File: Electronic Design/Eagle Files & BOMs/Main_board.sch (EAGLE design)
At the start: 42 parts, among them IC2 ATMEGA328-PU, IC3 LM2576S, Q1 IRF9540, Q2 IRF9540, X1 16MHz

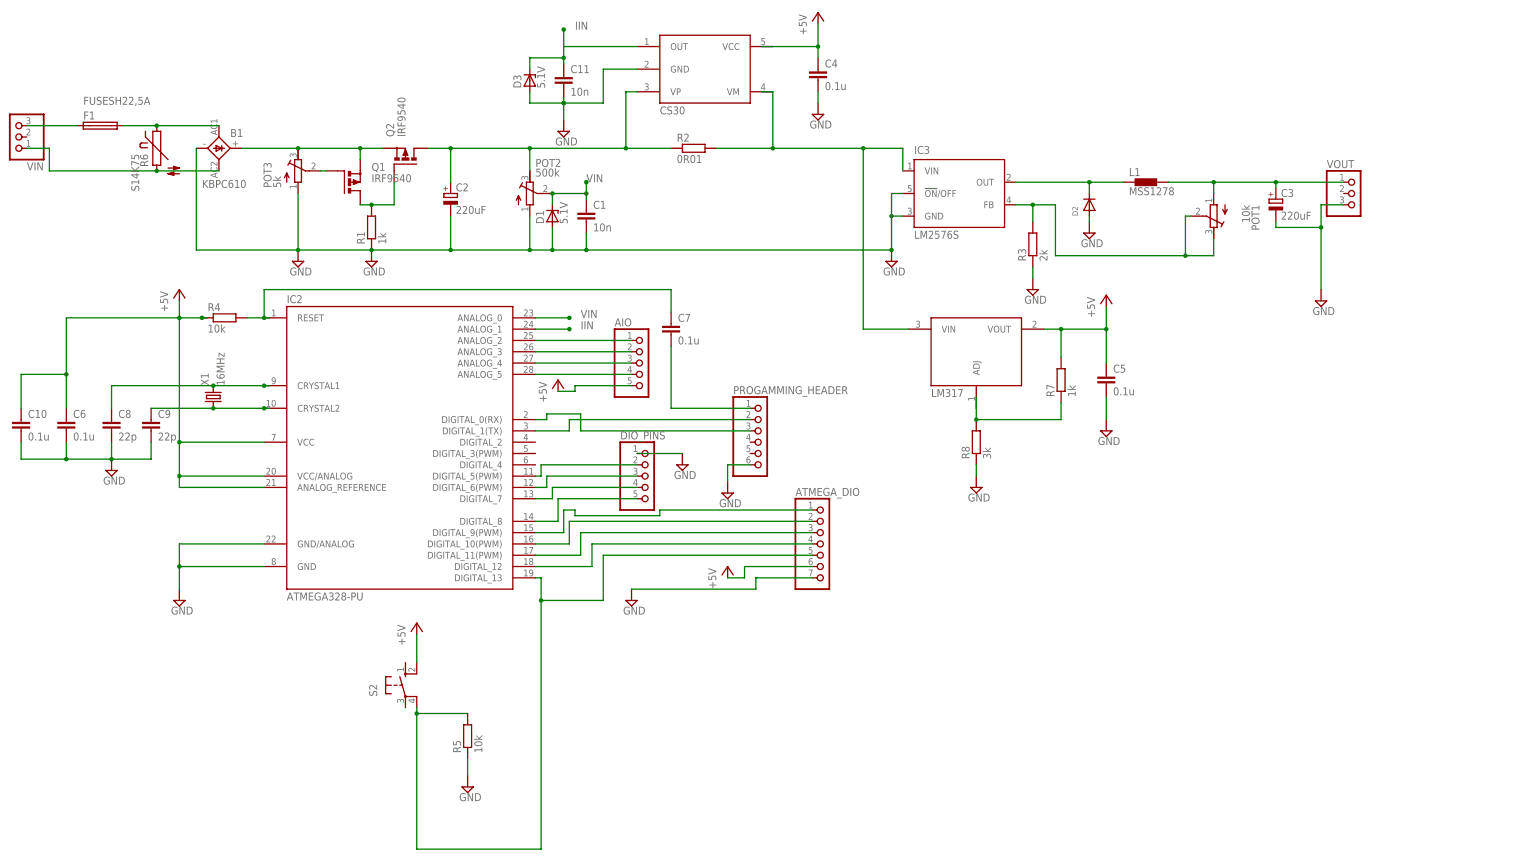
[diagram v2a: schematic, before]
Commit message: adding hardwired voltage divider for Vin measurement
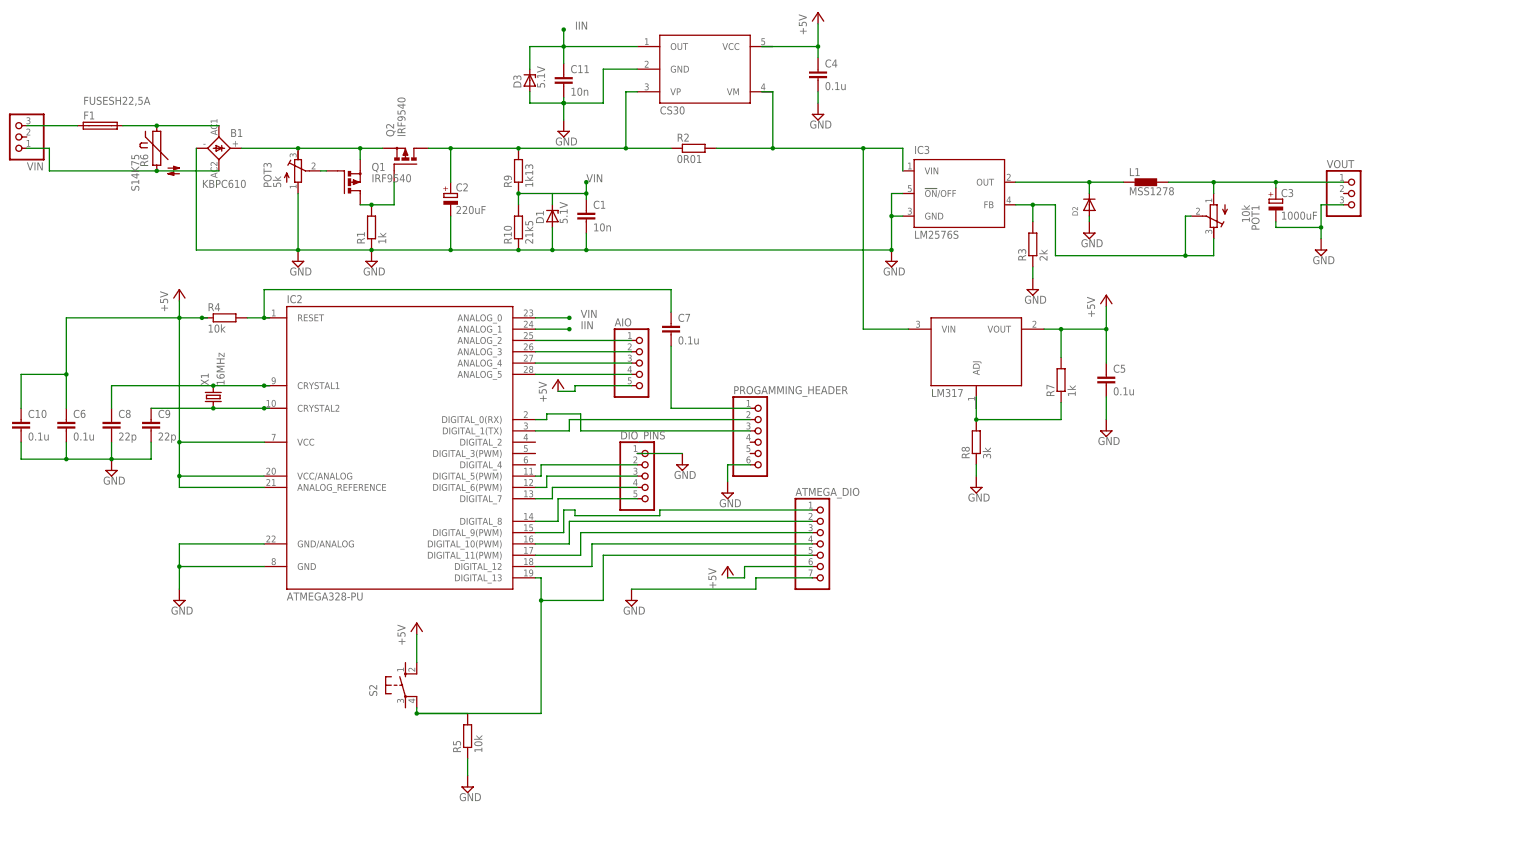
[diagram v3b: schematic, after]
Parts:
- removed POT2: 500k, resistor:R-TRIMM3296W
- added R10: 21k5, resistor:R-EU_R0805
- added R9: 1k13, resistor:R-EU_R0805
- C3: value 220uF -> 1000uF
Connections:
- net GND: now also R10.1; no longer POT2.A
- net N$3: now also R9.2; no longer POT2.E
- net VIN: now also R10.2, R9.1; no longer POT2.S
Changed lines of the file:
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@@
 <part name="C1" library="resistor" deviceset="C-EU" device="C1206K" value="10n"/>
 <part name="C2" library="resistor" deviceset="CPOL-EU" device="E3.5-10" value="220uF"/>
-<part name="POT2" library="resistor" deviceset="R-TRIMM" device="3296W" value="500k"/>
 <part name="Q1" library="transistor-power" deviceset="PMOSFET_P" device="TO220BH" value="IRF9540"/>
 <part name="Q2" library="transistor-power" deviceset="PMOSFET_P" device="TO220BH" value="IRF9540"/>
@@
 <part name="L1" library="Samson" deviceset="MSS1278" device=""/>
 <part name="SUPPLY9" library="supply2" deviceset="GND" device=""/>
-<part name="C3" library="resistor" deviceset="CPOL-EU" device="E3.5-10" value="220uF"/>
+<part name="C3" library="resistor" deviceset="CPOL-EU" device="E3.5-10" value="1000uF"/>
 <part name="C4" library="resistor" deviceset="C-EU" device="C1206K" value="0.1u"/>
 <part name="C5" library="resistor" deviceset="C-EU" device="C1206K" value="0.1u"/>
@@
 <part name="C11" library="resistor" deviceset="C-EU" device="C1206K" value="10n"/>
 <part name="D3" library="diode" deviceset="ZPD" device="" value="5.1V"/>
+<part name="R9" library="resistor" deviceset="R-EU_" device="R0805" value="1k13"/>
+<part name="R10" library="resistor" deviceset="R-EU_" device="R0805" value="21k5"/>
 </parts>
 <sheets>
@@
 <instance part="C1" gate="G$1" x="-1.27" y="74.93"/>
 <instance part="C2" gate="G$1" x="-31.75" y="78.74"/>
-<instance part="POT2" gate="G$1" x="-13.97" y="78.74" smashed="yes">
-<attribute name="NAME" x="-12.7" y="84.709" size="1.778" layer="95"/>
-<attribute name="VALUE" x="-12.7" y="82.55" size="1.778" layer="96"/>
-</instance>
 <instance part="Q1" gate="G$1" x="-54.61" y="81.28"/>
 <instance part="Q2" gate="G$1" x="-41.91" y="86.36" rot="R90"/>
@@
 <instance part="DIO_PINS" gate="A" x="12.7" y="15.24"/>
 <instance part="SUPPLY5" gate="GND" x="20.32" y="17.78"/>
-<instance part="SUPPLY2" gate="GND" x="163.83" y="54.61"/>
+<instance part="SUPPLY2" gate="GND" x="163.83" y="66.04"/>
 <instance part="SUPPLY4" gate="GND" x="86.36" y="12.7"/>
 <instance part="+3V1" gate="1" x="115.57" y="55.88"/>
@@
 <instance part="C11" gate="G$1" x="-6.35" y="105.41"/>
 <instance part="D3" gate="G$1" x="-13.97" y="104.14" rot="R90"/>
+<instance part="R9" gate="G$1" x="-16.51" y="83.82" rot="R90"/>
+<instance part="R10" gate="G$1" x="-16.51" y="71.12" rot="R90"/>
 </instances>
 <busses>
@@
 <label x="-1.27" y="81.28" size="1.778" layer="95"/>
 <pinref part="C1" gate="G$1" pin="1"/>
-<pinref part="POT2" gate="G$1" pin="S"/>
 <wire x1="-1.27" y1="78.74" x2="-1.27" y2="81.28" width="0.1524" layer="91"/>
 <wire x1="-8.89" y1="76.2" x2="-8.89" y2="78.74" width="0.1524" layer="91"/>
 <wire x1="-8.89" y1="78.74" x2="-1.27" y2="78.74" width="0.1524" layer="91"/>
 <junction x="-1.27" y="78.74"/>
-<junction x="-8.89" y="78.74"/>
 <pinref part="D1" gate="G$1" pin="C"/>
+<pinref part="R9" gate="G$1" pin="1"/>
+<wire x1="-8.89" y1="78.74" x2="-16.51" y2="78.74" width="0.1524" layer="91"/>
+<pinref part="R10" gate="G$1" pin="2"/>
+<wire x1="-16.51" y1="78.74" x2="-16.51" y2="76.2" width="0.1524" layer="91"/>
+<junction x="-16.51" y="78.74"/>
 </segment>
 <segment>
@@
 <pinref part="C11" gate="G$1" pin="1"/>
 <wire x1="-6.35" y1="111.76" x2="-6.35" y2="115.57" width="0.1524" layer="91"/>
-<wire x1="-6.35" y1="111.76" x2="-6.35" y2="109.22" width="0.1524" layer="91"/>
 <pinref part="D3" gate="G$1" pin="C"/>
-<wire x1="-6.35" y1="109.22" x2="-6.35" y2="107.95" width="0.1524" layer="91"/>
-<wire x1="-13.97" y1="106.68" x2="-13.97" y2="109.22" width="0.1524" layer="91"/>
-<wire x1="-13.97" y1="109.22" x2="-6.35" y2="109.22" width="0.1524" layer="91"/>
-<junction x="-6.35" y="109.22"/>
+<wire x1="-6.35" y1="111.76" x2="-6.35" y2="107.95" width="0.1524" layer="91"/>
+<wire x1="-13.97" y1="106.68" x2="-13.97" y2="111.76" width="0.1524" layer="91"/>
+<wire x1="-13.97" y1="111.76" x2="-6.35" y2="111.76" width="0.1524" layer="91"/>
+<junction x="-6.35" y="111.76"/>
 </segment>
 </net>
@@
 <wire x1="-88.9" y1="88.9" x2="-88.9" y2="66.04" width="0.1524" layer="91"/>
 <wire x1="-66.04" y1="66.04" x2="-88.9" y2="66.04" width="0.1524" layer="91"/>
-<wire x1="-13.97" y1="66.04" x2="-8.89" y2="66.04" width="0.1524" layer="91"/>
 <wire x1="-8.89" y1="66.04" x2="-1.27" y2="66.04" width="0.1524" layer="91"/>
 <wire x1="-8.89" y1="71.12" x2="-8.89" y2="66.04" width="0.1524" layer="91"/>
 <pinref part="C1" gate="G$1" pin="2"/>
 <wire x1="-1.27" y1="69.85" x2="-1.27" y2="66.04" width="0.1524" layer="91"/>
-<pinref part="POT2" gate="G$1" pin="A"/>
-<wire x1="-13.97" y1="73.66" x2="-13.97" y2="66.04" width="0.1524" layer="91"/>
-<junction x="-13.97" y="66.04"/>
 <junction x="-8.89" y="66.04"/>
 <junction x="-1.27" y="66.04"/>
 <pinref part="D1" gate="G$1" pin="A"/>
 <wire x1="-49.53" y1="66.04" x2="-31.75" y2="66.04" width="0.1524" layer="91"/>
-<wire x1="-31.75" y1="66.04" x2="-13.97" y2="66.04" width="0.1524" layer="91"/>
+<wire x1="-31.75" y1="66.04" x2="-16.51" y2="66.04" width="0.1524" layer="91"/>
+<wire x1="-16.51" y1="66.04" x2="-8.89" y2="66.04" width="0.1524" layer="91"/>
 <wire x1="-1.27" y1="66.04" x2="67.31" y2="66.04" width="0.1524" layer="91"/>
 <pinref part="C2" gate="G$1" pin="-"/>
@@
 <pinref part="SUPPLY7" gate="GND" pin="GND"/>
 <junction x="67.31" y="66.04"/>
+<pinref part="R10" gate="G$1" pin="1"/>
+<junction x="-16.51" y="66.04"/>
 </segment>
 <segment>
@@
 <wire x1="163.83" y1="76.2" x2="163.83" y2="71.12" width="0.1524" layer="91"/>
 <pinref part="C3" gate="G$1" pin="-"/>
-<wire x1="163.83" y1="71.12" x2="163.83" y2="57.15" width="0.1524" layer="91"/>
+<wire x1="163.83" y1="71.12" x2="163.83" y2="68.58" width="0.1524" layer="91"/>
 <wire x1="153.67" y1="72.39" x2="153.67" y2="71.12" width="0.1524" layer="91"/>
 <wire x1="153.67" y1="71.12" x2="163.83" y2="71.12" width="0.1524" layer="91"/>
@@
 <net name="N$3" class="0">
 <segment>
-<pinref part="POT2" gate="G$1" pin="E"/>
-<wire x1="-13.97" y1="88.9" x2="-13.97" y2="83.82" width="0.1524" layer="91"/>
 <pinref part="Q2" gate="G$1" pin="D"/>
 <wire x1="-36.83" y1="88.9" x2="-31.75" y2="88.9" width="0.1524" layer="91"/>
 <pinref part="C2" gate="G$1" pin="+"/>
-<wire x1="-31.75" y1="88.9" x2="-13.97" y2="88.9" width="0.1524" layer="91"/>
 <wire x1="-31.75" y1="88.9" x2="-31.75" y2="81.28" width="0.1524" layer="91"/>
 <junction x="-31.75" y="88.9"/>
 <pinref part="R2" gate="G$1" pin="1"/>
-<wire x1="-13.97" y1="88.9" x2="7.62" y2="88.9" width="0.1524" layer="91"/>
+<wire x1="-31.75" y1="88.9" x2="-16.51" y2="88.9" width="0.1524" layer="91"/>
+<wire x1="-16.51" y1="88.9" x2="7.62" y2="88.9" width="0.1524" layer="91"/>
 <wire x1="7.62" y1="88.9" x2="17.78" y2="88.9" width="0.1524" layer="91"/>
 <wire x1="10.16" y1="101.6" x2="7.62" y2="101.6" width="0.1524" layer="91"/>
@@
 <junction x="7.62" y="88.9"/>
 <pinref part="U$2" gate="G$1" pin="VP"/>
-<junction x="-13.97" y="88.9"/>
+<pinref part="R9" gate="G$1" pin="2"/>
+<junction x="-16.51" y="88.9"/>
 </segment>
 </net>
@@
 <wire x1="-12.7" y1="-7.62" x2="-11.43" y2="-7.62" width="0.1524" layer="91"/>
 <wire x1="-11.43" y1="-7.62" x2="-11.43" y2="-12.7" width="0.1524" layer="91"/>
-<wire x1="-11.43" y1="-12.7" x2="-11.43" y2="-68.58" width="0.1524" layer="91"/>
-<wire x1="-11.43" y1="-68.58" x2="-39.37" y2="-68.58" width="0.1524" layer="91"/>
-<wire x1="-39.37" y1="-68.58" x2="-39.37" y2="-38.1" width="0.1524" layer="91"/>
+<wire x1="-11.43" y1="-12.7" x2="-11.43" y2="-38.1" width="0.1524" layer="91"/>
+<wire x1="-11.43" y1="-38.1" x2="-39.37" y2="-38.1" width="0.1524" layer="91"/>
 <pinref part="R5" gate="G$1" pin="2"/>
 <wire x1="-27.94" y1="-38.1" x2="-39.37" y2="-38.1" width="0.1524" layer="91"/>

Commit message: adding new layout of PCB
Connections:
- new net BUTTON: IC2.DIGITAL_2, R5.2, S2.P1
- net N$8: no longer R5.2, S2.P1
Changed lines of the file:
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@@
 <wire x1="-12.7" y1="-7.62" x2="-11.43" y2="-7.62" width="0.1524" layer="91"/>
 <wire x1="-11.43" y1="-7.62" x2="-11.43" y2="-12.7" width="0.1524" layer="91"/>
-<wire x1="-11.43" y1="-12.7" x2="-11.43" y2="-38.1" width="0.1524" layer="91"/>
-<wire x1="-11.43" y1="-38.1" x2="-39.37" y2="-38.1" width="0.1524" layer="91"/>
-<pinref part="R5" gate="G$1" pin="2"/>
-<wire x1="-27.94" y1="-38.1" x2="-39.37" y2="-38.1" width="0.1524" layer="91"/>
 <wire x1="2.54" y1="-2.54" x2="2.54" y2="-12.7" width="0.1524" layer="91"/>
 <wire x1="2.54" y1="-12.7" x2="-11.43" y2="-12.7" width="0.1524" layer="91"/>
-<junction x="-11.43" y="-12.7"/>
 <pinref part="ATMEGA_DIO" gate="A" pin="5"/>
 <wire x1="49.53" y1="-2.54" x2="2.54" y2="-2.54" width="0.1524" layer="91"/>
-<pinref part="S2" gate="1" pin="P1"/>
-<wire x1="-39.37" y1="-36.83" x2="-39.37" y2="-38.1" width="0.1524" layer="91"/>
-<junction x="-39.37" y="-38.1"/>
 </segment>
 </net>
@@
 </segment>
 </net>
+<net name="BUTTON" class="0">
+<segment>
+<pinref part="IC2" gate="1" pin="DIGITAL_2"/>
+<wire x1="-12.7" y1="22.86" x2="-8.89" y2="22.86" width="0.1524" layer="91"/>
+<junction x="-8.89" y="22.86"/>
+<label x="-7.62" y="21.59" size="1.778" layer="95"/>
+</segment>
+<segment>
+<pinref part="R5" gate="G$1" pin="2"/>
+<wire x1="-27.94" y1="-38.1" x2="-39.37" y2="-38.1" width="0.1524" layer="91"/>
+<pinref part="S2" gate="1" pin="P1"/>
+<wire x1="-39.37" y1="-36.83" x2="-39.37" y2="-38.1" width="0.1524" layer="91"/>
+<junction x="-39.37" y="-38.1"/>
+<wire x1="-11.43" y1="-38.1" x2="-39.37" y2="-38.1" width="0.1524" layer="91"/>
+<junction x="-11.43" y="-38.1"/>
+<label x="-8.89" y="-38.1" size="1.778" layer="95"/>
+</segment>
+</net>

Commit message: adding ground to AIO and general tidy up
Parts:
- AIO: device pinhead:PINHD-1X5 -> pinhead:PINHD-1X6
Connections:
- net GND: now also AIO.6
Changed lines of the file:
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@@
 <part name="C6" library="resistor" deviceset="C-EU" device="C1206K" value="0.1u"/>
 <part name="C10" library="resistor" deviceset="C-EU" device="C1206K" value="0.1u"/>
-<part name="AIO" library="pinhead" deviceset="PINHD-1X5" device=""/>
+<part name="AIO" library="pinhead" deviceset="PINHD-1X6" device=""/>
 <part name="+5V4" library="supply1" deviceset="+5V" device=""/>
 <part name="R2" library="resistor" deviceset="R-EU_" device="M1206" value="0R01"/>
@@
 <part name="R9" library="resistor" deviceset="R-EU_" device="R0805" value="1k13"/>
 <part name="R10" library="resistor" deviceset="R-EU_" device="R0805" value="21k5"/>
+<part name="SUPPLY12" library="supply2" deviceset="GND" device=""/>
 </parts>
 <sheets>
@@
 <instance part="C6" gate="G$1" x="-118.11" y="27.94"/>
 <instance part="C10" gate="G$1" x="-128.27" y="27.94"/>
-<instance part="AIO" gate="A" x="11.43" y="40.64"/>
+<instance part="AIO" gate="A" x="11.43" y="38.1"/>
 <instance part="+5V4" gate="1" x="-7.62" y="36.83"/>
 <instance part="R2" gate="G$1" x="22.86" y="88.9"/>
@@
 <instance part="R9" gate="G$1" x="-16.51" y="83.82" rot="R90"/>
 <instance part="R10" gate="G$1" x="-16.51" y="71.12" rot="R90"/>
+<instance part="SUPPLY12" gate="GND" x="1.27" y="31.75"/>
 </instances>
 <busses>
@@
 <wire x1="-16.51" y1="78.74" x2="-16.51" y2="76.2" width="0.1524" layer="91"/>
 <junction x="-16.51" y="78.74"/>
+<junction x="-8.89" y="78.74"/>
 </segment>
 <segment>
@@
 <pinref part="SUPPLY11" gate="GND" pin="GND"/>
 </segment>
+<segment>
+<pinref part="SUPPLY12" gate="GND" pin="GND"/>
+<wire x1="1.27" y1="34.29" x2="6.35" y2="34.29" width="0.1524" layer="91"/>
+<wire x1="6.35" y1="34.29" x2="6.35" y2="33.02" width="0.1524" layer="91"/>
+<pinref part="AIO" gate="A" pin="6"/>
+<wire x1="6.35" y1="33.02" x2="8.89" y2="33.02" width="0.1524" layer="91"/>
+</segment>
 </net>
 <net name="M1S" class="0">
@@
 <pinref part="+3V2" gate="1" pin="+5V"/>
 <pinref part="U$2" gate="G$1" pin="VCC"/>
-<wire x1="38.1" y1="111.76" x2="40.64" y2="111.76" width="0.1524" layer="91"/>
 <wire x1="50.8" y1="111.76" x2="40.64" y2="111.76" width="0.1524" layer="91"/>
 <pinref part="C4" gate="G$1" pin="1"/>

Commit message: Moving fuse close to output rather than input
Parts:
- R10: value 21k5 -> 1k13
- R9: value 1k13 -> 21k5
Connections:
- removed net N$18: B1.AC1, F1.2, R6.1
- new net N$2: F1.2, VOUT.1
- net N$1: now also B1.AC1, R6.1; no longer F1.1
- net N$24: now also F1.1; no longer VOUT.1
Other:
- moved on the sheet: F1, VOUT
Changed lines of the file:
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@@
 <part name="C11" library="resistor" deviceset="C-EU" device="C1206K" value="10n"/>
 <part name="D3" library="diode" deviceset="ZPD" device="" value="5.1V"/>
-<part name="R9" library="resistor" deviceset="R-EU_" device="R0805" value="1k13"/>
-<part name="R10" library="resistor" deviceset="R-EU_" device="R0805" value="21k5"/>
+<part name="R9" library="resistor" deviceset="R-EU_" device="R0805" value="21k5"/>
+<part name="R10" library="resistor" deviceset="R-EU_" device="R0805" value="1k13"/>
 <part name="SUPPLY12" library="supply2" deviceset="GND" device=""/>
 </parts>
@@
 <instance part="SUPPLY23" gate="GND" x="-66.04" y="63.5"/>
 <instance part="VIN" gate="A" x="-129.54" y="91.44" rot="R180"/>
-<instance part="F1" gate="G$1" x="-110.49" y="93.98" smashed="yes">
-<attribute name="NAME" x="-114.3" y="95.377" size="1.778" layer="95"/>
-<attribute name="VALUE" x="-114.3" y="98.679" size="1.778" layer="96"/>
+<instance part="F1" gate="G$1" x="171.45" y="81.28" smashed="yes">
+<attribute name="NAME" x="167.64" y="82.677" size="1.778" layer="95"/>
+<attribute name="VALUE" x="167.64" y="85.979" size="1.778" layer="96"/>
 </instance>
 <instance part="SUPPLY29" gate="GND" x="-92.71" y="-12.7"/>
@@
 <instance part="SUPPLY4" gate="GND" x="86.36" y="12.7"/>
 <instance part="+3V1" gate="1" x="115.57" y="55.88"/>
-<instance part="VOUT" gate="A" x="171.45" y="78.74"/>
+<instance part="VOUT" gate="A" x="195.58" y="78.74"/>
 <instance part="C6" gate="G$1" x="-118.11" y="27.94"/>
 <instance part="C10" gate="G$1" x="-128.27" y="27.94"/>
@@
 <pinref part="SUPPLY2" gate="GND" pin="GND"/>
 <pinref part="VOUT" gate="A" pin="3"/>
-<wire x1="168.91" y1="76.2" x2="163.83" y2="76.2" width="0.1524" layer="91"/>
+<wire x1="193.04" y1="76.2" x2="163.83" y2="76.2" width="0.1524" layer="91"/>
 <wire x1="163.83" y1="76.2" x2="163.83" y2="71.12" width="0.1524" layer="91"/>
 <pinref part="C3" gate="G$1" pin="-"/>
@@
 </segment>
 </net>
-<net name="N$1" class="0">
-<segment>
-<pinref part="VIN" gate="A" pin="3"/>
-<pinref part="F1" gate="G$1" pin="1"/>
-<wire x1="-127" y1="93.98" x2="-115.57" y2="93.98" width="0.1524" layer="91"/>
-</segment>
-</net>
-<net name="N$18" class="0">
-<segment>
-<pinref part="F1" gate="G$1" pin="2"/>
-<pinref part="R6" gate="G$1" pin="1"/>
-<wire x1="-105.41" y1="93.98" x2="-97.79" y2="93.98" width="0.1524" layer="91"/>
-<pinref part="B1" gate="1" pin="AC1"/>
-<wire x1="-83.82" y1="93.98" x2="-97.79" y2="93.98" width="0.1524" layer="91"/>
-<junction x="-97.79" y="93.98"/>
-</segment>
-</net>
 <net name="ANALOG_3" class="0">
 <segment>
@@
 <wire x1="139.7" y1="81.28" x2="153.67" y2="81.28" width="0.1524" layer="91"/>
 <wire x1="153.67" y1="81.28" x2="153.67" y2="80.01" width="0.1524" layer="91"/>
-<pinref part="VOUT" gate="A" pin="1"/>
-<wire x1="153.67" y1="81.28" x2="168.91" y2="81.28" width="0.1524" layer="91"/>
+<junction x="139.7" y="81.28"/>
+<pinref part="F1" gate="G$1" pin="1"/>
+<wire x1="166.37" y1="81.28" x2="153.67" y2="81.28" width="0.1524" layer="91"/>
 <junction x="153.67" y="81.28"/>
-<junction x="139.7" y="81.28"/>
 </segment>
 </net>
@@
 </segment>
 </net>
+<net name="N$1" class="0">
+<segment>
+<pinref part="VIN" gate="A" pin="3"/>
+<wire x1="-127" y1="93.98" x2="-97.79" y2="93.98" width="0.1524" layer="91"/>
+<pinref part="R6" gate="G$1" pin="1"/>
+<pinref part="B1" gate="1" pin="AC1"/>
+<wire x1="-83.82" y1="93.98" x2="-97.79" y2="93.98" width="0.1524" layer="91"/>
+<junction x="-97.79" y="93.98"/>
+</segment>
+</net>
+<net name="N$2" class="0">
+<segment>
+<pinref part="F1" gate="G$1" pin="2"/>
+<pinref part="VOUT" gate="A" pin="1"/>
+<wire x1="176.53" y1="81.28" x2="193.04" y2="81.28" width="0.1524" layer="91"/>
+</segment>
+</net>

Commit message: adding 5.1v zeners and LEDs to outputs of voltage regulators
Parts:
- added D4, D5: 5.1V, diode:ZPD
- added LED1, LED2: (no value), adafruit:LEDSMT1206
- added R11, R12: 2k, resistor:R-EU_R1206
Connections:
- new net N$18: LED2.A, R11.1
- new net N$28: LED1.C, R12.2
- net +5V: now also D4.C, LED1.A
- net GND: now also D4.A, D5.A, LED2.C, R12.1
- net N$2: now also F1.1, L1.2, POT1.A; no longer F1.2, VOUT.1
- net N$24: now also D5.C, F1.2, R11.2, VOUT.1; no longer F1.1, L1.2, POT1.A
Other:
- moved on the sheet: C3, C5, F1, VOUT
